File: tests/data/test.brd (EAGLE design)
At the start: 24.4 x 15.7 mm, 2 parts

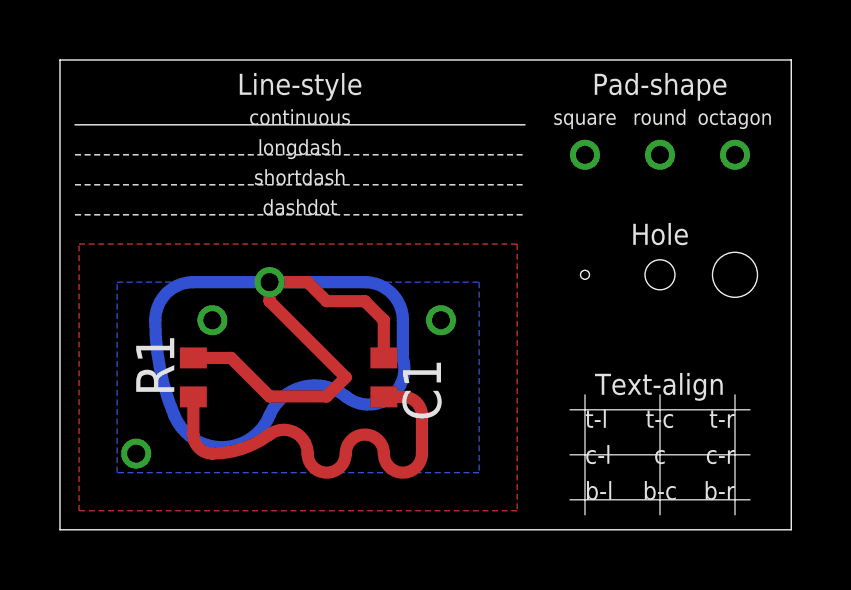
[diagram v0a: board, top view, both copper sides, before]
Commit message: Update test data
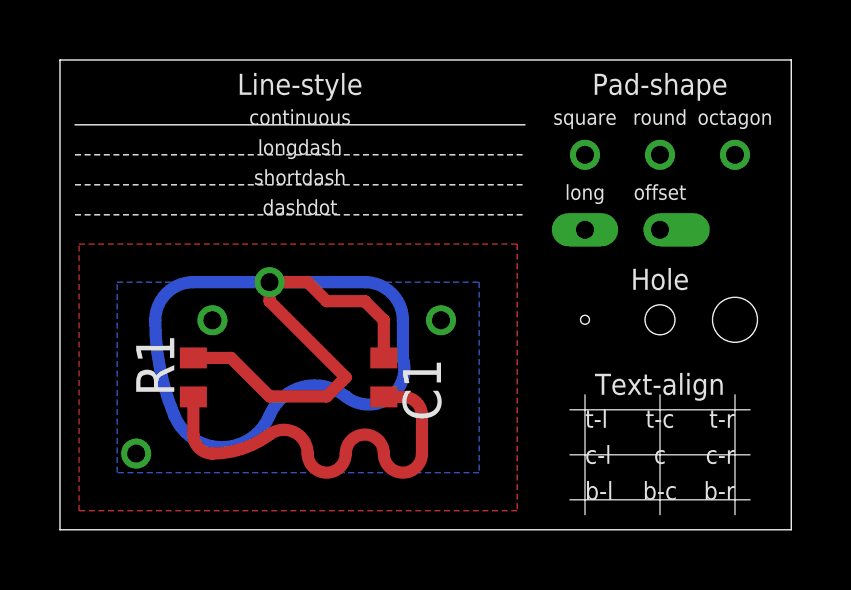
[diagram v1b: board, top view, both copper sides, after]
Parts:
- added U$1: PADLONG, pad:LONG
- added U$2: PADOFFSET, pad:OFFSET
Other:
- board text added: "long"
- board text added: "offset"
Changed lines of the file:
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@@
 <text x="20" y="13.5" size="0.5" layer="21" align="bottom-center">round</text>
 <text x="22.5" y="13.5" size="0.5" layer="21" align="bottom-center">octagon</text>
-<hole x="20" y="8.5" drill="1"/>
-<text x="20" y="9.5" size="0.7" layer="21" align="bottom-center">Hole</text>
-<hole x="17.5" y="8.5" drill="0.3"/>
-<hole x="22.5" y="8.5" drill="1.5"/>
+<hole x="20" y="7" drill="1"/>
+<text x="20" y="8" size="0.7" layer="21" align="bottom-center">Hole</text>
+<hole x="17.5" y="7" drill="0.3"/>
+<hole x="22.5" y="7" drill="1.5"/>
+<text x="17.5" y="11" size="0.5" layer="21" align="bottom-center">long</text>
+<text x="20" y="11" size="0.5" layer="21" align="bottom-center">offset</text>
 </plain>
 <attributes>
@@
 <element name="C1" library="rcl" package="C0402" value="1u" x="10.795" y="5.08" rot="R270"/>
 <element name="R1" library="rcl" package="R0402" value="1k" x="4.445" y="5.08" rot="R90"/>
+<element name="U$1" library="pad" package="LONG" value="PADLONG" x="17.5" y="10"/>
+<element name="U$2" library="pad" package="OFFSET" value="PADOFFSET" x="20" y="10"/>
 </elements>
 <signals>
@@
 <signal name="N$4">
 <via x="20" y="12.5" extent="1-16" drill="0.6"/>
+<wire x1="20" y1="10" x2="20" y2="10" width="0" layer="19" extent="1-16"/>
 </signal>
 <signal name="N$5">

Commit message: Render long and offset pad
also fix pad rotate
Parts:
- renumbered U$1 to PAD1, U$2 to PAD2
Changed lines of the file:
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@@
 <element name="C1" library="rcl" package="C0402" value="1u" x="10.795" y="5.08" rot="R270"/>
 <element name="R1" library="rcl" package="R0402" value="1k" x="4.445" y="5.08" rot="R90"/>
-<element name="U$1" library="pad" package="LONG" value="PADLONG" x="17.5" y="10"/>
-<element name="U$2" library="pad" package="OFFSET" value="PADOFFSET" x="20" y="10"/>
+<element name="PAD1" library="pad" package="LONG" value="PADLONG" x="17.5" y="10"/>
+<element name="PAD2" library="pad" package="OFFSET" value="PADOFFSET" x="20" y="10"/>
 </elements>
 <signals>

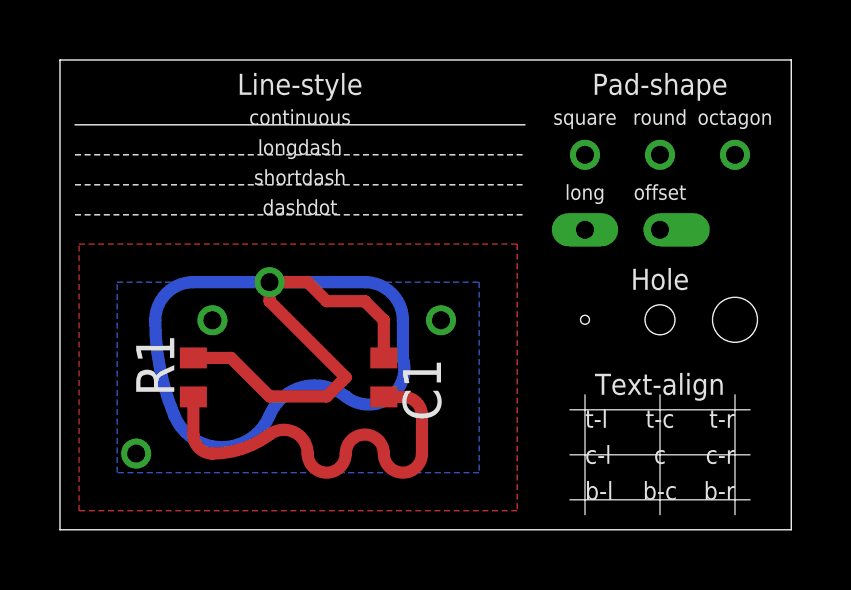
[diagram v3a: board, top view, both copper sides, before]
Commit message: Add rotated pad to test data
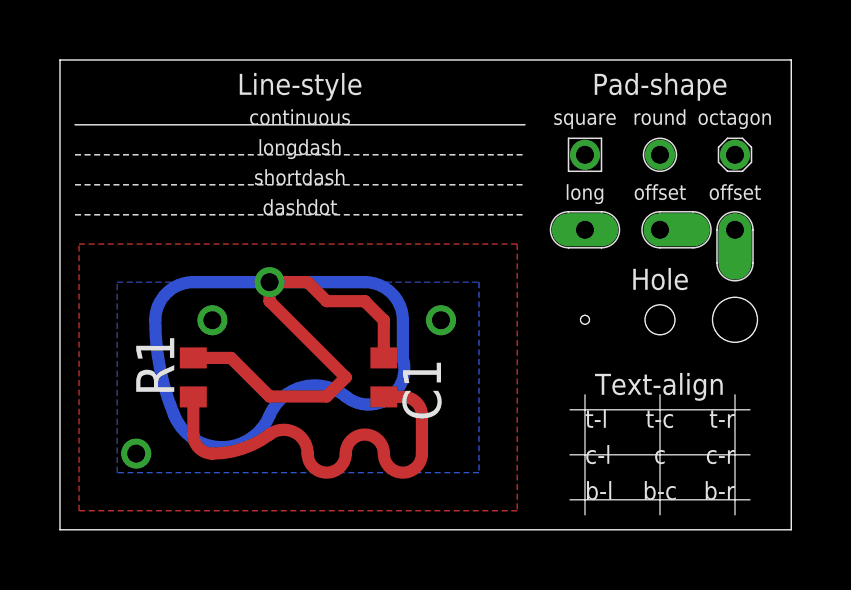
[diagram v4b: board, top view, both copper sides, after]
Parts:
- added PAD3: PADOFFSET, pad:OFFSET
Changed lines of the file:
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@@
 <setting verticaltext="up"/>
 </settings>
-<grid distance="0.5" unitdist="mm" unit="mm" style="lines" multiple="1" display="no" altdistance="0.025" altunitdist="inch" altunit="inch"/>
+<grid distance="0.05" unitdist="mm" unit="mm" style="lines" multiple="1" display="no" altdistance="0.025" altunitdist="inch" altunit="inch"/>
 <layers>
 <layer number="1" name="Top" color="4" fill="1" visible="yes" active="yes"/>
@@
 <text x="17.5" y="11" size="0.5" layer="21" align="bottom-center">long</text>
 <text x="20" y="11" size="0.5" layer="21" align="bottom-center">offset</text>
+<text x="22.5" y="11" size="0.5" layer="21" align="bottom-center">offset</text>
+<wire x1="23.1" y1="10" x2="23.1" y2="8.9" width="0.05" layer="21"/>
+<wire x1="23.1" y1="8.9" x2="21.9" y2="8.9" width="0.05" layer="21" curve="-180"/>
+<wire x1="21.9" y1="8.9" x2="21.9" y2="10" width="0.05" layer="21"/>
+<wire x1="21.9" y1="10" x2="23.1" y2="10" width="0.05" layer="21" curve="-180"/>
+<wire x1="20" y1="10.6" x2="21.1" y2="10.6" width="0.05" layer="21"/>
+<wire x1="21.1" y1="10.6" x2="21.1" y2="9.4" width="0.05" layer="21" curve="-180"/>
+<wire x1="21.1" y1="9.4" x2="20" y2="9.4" width="0.05" layer="21"/>
+<wire x1="20" y1="9.4" x2="20" y2="10.6" width="0.05" layer="21" curve="-180"/>
+<wire x1="16.95" y1="10.6" x2="18.05" y2="10.6" width="0.05" layer="21"/>
+<wire x1="18.05" y1="10.6" x2="18.05" y2="9.4" width="0.05" layer="21" curve="-180"/>
+<wire x1="18.05" y1="9.4" x2="16.95" y2="9.4" width="0.05" layer="21"/>
+<wire x1="16.95" y1="9.4" x2="16.95" y2="10.6" width="0.05" layer="21" curve="-180"/>
+<wire x1="16.95" y1="13.05" x2="18.05" y2="13.05" width="0.05" layer="21"/>
+<wire x1="18.05" y1="13.05" x2="18.05" y2="11.95" width="0.05" layer="21"/>
+<wire x1="18.05" y1="11.95" x2="16.95" y2="11.95" width="0.05" layer="21"/>
+<wire x1="16.95" y1="11.95" x2="16.95" y2="13.05" width="0.05" layer="21"/>
+<wire x1="19.45" y1="12.5" x2="20.55" y2="12.5" width="0.05" layer="21" curve="-180"/>
+<wire x1="20.55" y1="12.5" x2="19.45" y2="12.5" width="0.05" layer="21" curve="-180"/>
+<wire x1="22.25" y1="13.05" x2="22.75" y2="13.05" width="0.05" layer="21"/>
+<wire x1="22.75" y1="13.05" x2="23.05" y2="12.75" width="0.05" layer="21"/>
+<wire x1="23.05" y1="12.75" x2="23.05" y2="12.25" width="0.05" layer="21"/>
+<wire x1="23.05" y1="12.25" x2="22.75" y2="11.95" width="0.05" layer="21"/>
+<wire x1="22.75" y1="11.95" x2="22.25" y2="11.95" width="0.05" layer="21"/>
+<wire x1="22.25" y1="11.95" x2="21.95" y2="12.25" width="0.05" layer="21"/>
+<wire x1="21.95" y1="12.25" x2="21.95" y2="12.75" width="0.05" layer="21"/>
+<wire x1="21.95" y1="12.75" x2="22.25" y2="13.05" width="0.05" layer="21"/>
 </plain>
 <attributes>
@@
 <element name="PAD1" library="pad" package="LONG" value="PADLONG" x="17.5" y="10"/>
 <element name="PAD2" library="pad" package="OFFSET" value="PADOFFSET" x="20" y="10"/>
+<element name="PAD3" library="pad" package="OFFSET" value="PADOFFSET" x="22.5" y="10" rot="R270"/>
 </elements>
 <signals>
